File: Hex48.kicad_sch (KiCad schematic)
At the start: 0 parts

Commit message: Begin adding schematic.
Board is much better designed by using a proper schematic instead of just a PCB. But to do that, we need lots of generic connectors, all connected together in a way that only makes sense on the physical PCB layout. Oh well, make a start.
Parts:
- added D1, D2: LED, LED_THT:LED_D10.0mm, symbol Device:LED
- added H1, H2, H3, H4, H5, H6: MountingHole, MountingHole:MountingHole_3.2mm_M3_Pad_TopBottom, symbol Mechanical:MountingHole
- added J1: Conn_02x24_Counter_Clockwise, Package_DIP:DIP-48_W15.24mm_Socket_LongPads, symbol Connector_Generic:Conn_02x24_Counter_Clockwise
- added J2, J3, J6: Conn_02x24_Odd_Even, Connector_PinSocket_2.54mm:PinSocket_2x24_P2.54mm_Vertical, symbol Connector_Generic:Conn_02x24_Odd_Even
- added J4, J5: Conn_02x02_Odd_Even, Connector_PinSocket_2.54mm:PinSocket_2x02_P2.54mm_Vertical, symbol Connector_Generic:Conn_02x02_Odd_Even
- added SW1, SW2: SW_Push, Button_Switch_THT:SW_PUSH_6mm, symbol Switch:SW_Push
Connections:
- new net: D1.1 (K), J4.1 (Pin_1), J4.3 (Pin_3), SW1.1
- new net: D1.2 (A), J4.2 (Pin_2), J4.4 (Pin_4), SW1.2
- new net: D2.1 (K), J5.1 (Pin_1), J5.3 (Pin_3), SW2.1
- new net: D2.2 (A), J5.2 (Pin_2), J5.4 (Pin_4), SW2.2
- new net: J1.40 (Pin_40), J2.17 (Pin_17), J2.18 (Pin_18)
- new net: J1.39 (Pin_39), J2.19 (Pin_19), J2.20 (Pin_20)
- new net: J1.38 (Pin_38), J2.21 (Pin_21), J2.22 (Pin_22)
- new net: J1.37 (Pin_37), J2.23 (Pin_23), J2.24 (Pin_24)
- new net: J1.36 (Pin_36), J2.25 (Pin_25), J2.26 (Pin_26)
- new net: J1.35 (Pin_35), J2.27 (Pin_27), J2.28 (Pin_28)
- new net: J1.34 (Pin_34), J2.29 (Pin_29), J2.30 (Pin_30)
- new net: J1.33 (Pin_33), J2.31 (Pin_31), J2.32 (Pin_32)
- new net: J1.32 (Pin_32), J2.33 (Pin_33), J2.34 (Pin_34)
- new net: J1.31 (Pin_31), J2.35 (Pin_35), J2.36 (Pin_36)
- new net: J1.30 (Pin_30), J2.37 (Pin_37), J2.38 (Pin_38)
- new net: J1.29 (Pin_29), J2.39 (Pin_39), J2.40 (Pin_40)
- new net: J1.28 (Pin_28), J2.41 (Pin_41), J2.42 (Pin_42)
- new net: J1.27 (Pin_27), J2.43 (Pin_43), J2.44 (Pin_44)
- new net: J1.26 (Pin_26), J2.45 (Pin_45), J2.46 (Pin_46)
- new net: J1.25 (Pin_25), J2.47 (Pin_47), J2.48 (Pin_48)
- new net: J1.9 (Pin_9), J3.17 (Pin_17), J3.18 (Pin_18)
- new net: J1.10 (Pin_10), J3.19 (Pin_19), J3.20 (Pin_20)
- new net: J1.11 (Pin_11), J3.21 (Pin_21), J3.22 (Pin_22)
- new net: J1.12 (Pin_12), J3.23 (Pin_23), J3.24 (Pin_24)
- new net: J1.13 (Pin_13), J3.25 (Pin_25), J3.26 (Pin_26)
- new net: J1.14 (Pin_14), J3.27 (Pin_27), J3.28 (Pin_28)
- new net: J1.15 (Pin_15), J3.29 (Pin_29), J3.30 (Pin_30)
- new net: J1.16 (Pin_16), J3.31 (Pin_31), J3.32 (Pin_32)
- new net: J1.17 (Pin_17), J3.33 (Pin_33), J3.34 (Pin_34)
- new net: J1.18 (Pin_18), J3.35 (Pin_35), J3.36 (Pin_36)
- new net: J1.19 (Pin_19), J3.37 (Pin_37), J3.38 (Pin_38)
- new net: J1.20 (Pin_20), J3.39 (Pin_39), J3.40 (Pin_40)
- new net: J1.21 (Pin_21), J3.41 (Pin_41), J3.42 (Pin_42)
- new net: J1.22 (Pin_22), J3.43 (Pin_43), J3.44 (Pin_44)
- new net: J1.23 (Pin_23), J3.45 (Pin_45), J3.46 (Pin_46)
- new net: J1.24 (Pin_24), J3.47 (Pin_47), J3.48 (Pin_48)
- new net pin1: J1.1 (Pin_1), J3.1 (Pin_1), J3.2 (Pin_2), J6.2 (Pin_2)
- new net pin2: J1.2 (Pin_2), J3.3 (Pin_3), J3.4 (Pin_4), J6.4 (Pin_4)
- new net pin3: J1.3 (Pin_3), J3.5 (Pin_5), J3.6 (Pin_6), J6.6 (Pin_6)
- new net pin4: J1.4 (Pin_4), J3.7 (Pin_7), J3.8 (Pin_8), J6.8 (Pin_8)
- new net pin41: J1.41 (Pin_41), J2.15 (Pin_15), J2.16 (Pin_16), J6.15 (Pin_15)
- new net pin42: J1.42 (Pin_42), J2.13 (Pin_13), J2.14 (Pin_14), J6.13 (Pin_13)
- new net pin43: J1.43 (Pin_43), J2.11 (Pin_11), J2.12 (Pin_12), J6.11 (Pin_11)
- new net pin44: J1.44 (Pin_44), J2.10 (Pin_10), J2.9 (Pin_9), J6.9 (Pin_9)
- new net pin45: J1.45 (Pin_45), J2.7 (Pin_7), J2.8 (Pin_8), J6.7 (Pin_7)
- new net pin46: J1.46 (Pin_46), J2.5 (Pin_5), J2.6 (Pin_6), J6.5 (Pin_5)
- new net pin47: J1.47 (Pin_47), J2.3 (Pin_3), J2.4 (Pin_4), J6.3 (Pin_3)
- new net pin48: J1.48 (Pin_48), J2.1 (Pin_1), J2.2 (Pin_2), J6.1 (Pin_1)
- new net pin5: J1.5 (Pin_5), J3.10 (Pin_10), J3.9 (Pin_9), J6.10 (Pin_10)
- new net pin6: J1.6 (Pin_6), J3.11 (Pin_11), J3.12 (Pin_12), J6.12 (Pin_12)
- new net pin7: J1.7 (Pin_7), J3.13 (Pin_13), J3.14 (Pin_14), J6.14 (Pin_14)
- new net pin8: J1.8 (Pin_8), J3.15 (Pin_15), J3.16 (Pin_16), J6.16 (Pin_16)

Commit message: Add title block info.
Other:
- company: (none) -> John Honniball
- title: (none) -> Hex48 Prototyping Board
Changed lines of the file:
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@@
 	(generator_version "8.0")
 	(paper "A4")
+	(title_block
+		(title "Hex48 Prototyping Board")
+		(date "2024-10-09")
+		(rev "0.2")
+		(company "John Honniball")
+		(comment 1 "Hexagonal DIL breadboard")
+	)
 	(junction
 		(at 106.68 76.2)

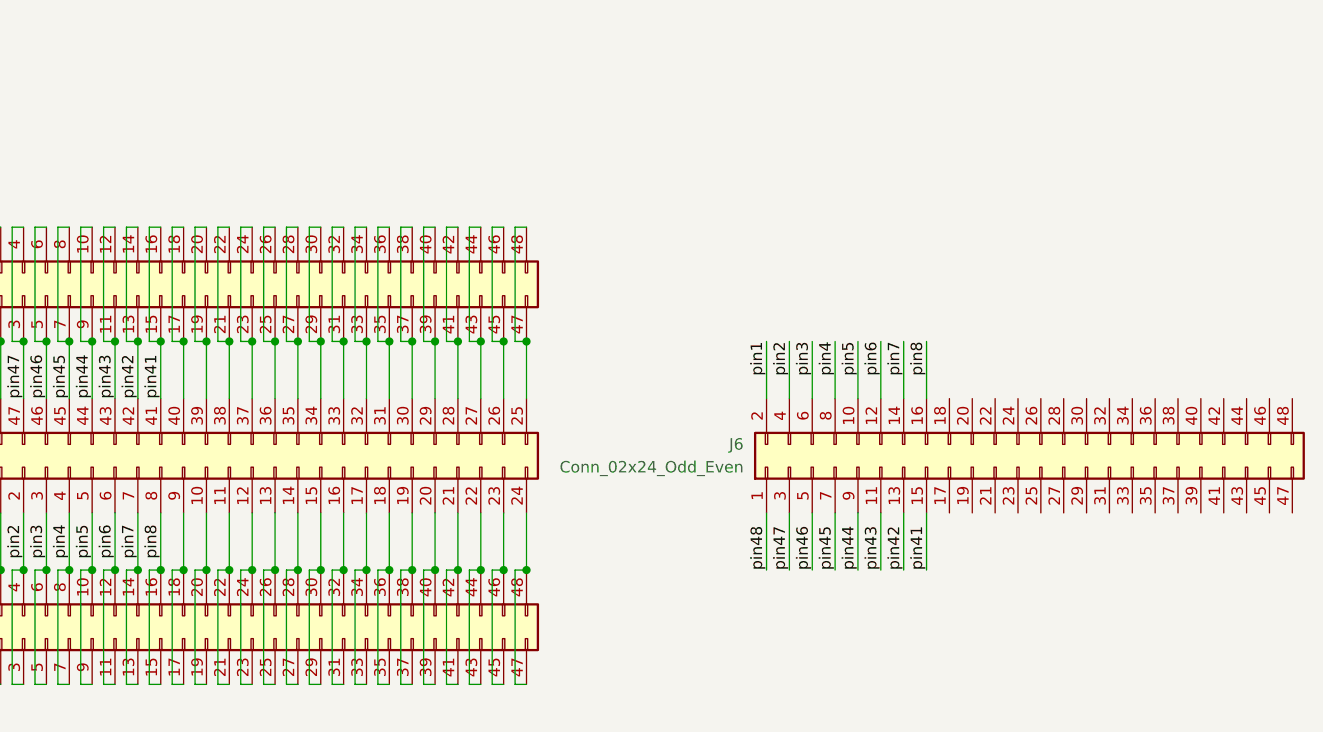
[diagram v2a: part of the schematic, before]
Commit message: Finish DIL wiring.
Place two 24-pin narrow DIL sockets and connect them to the 48-pin wide DIL socket. Name all pin signals.
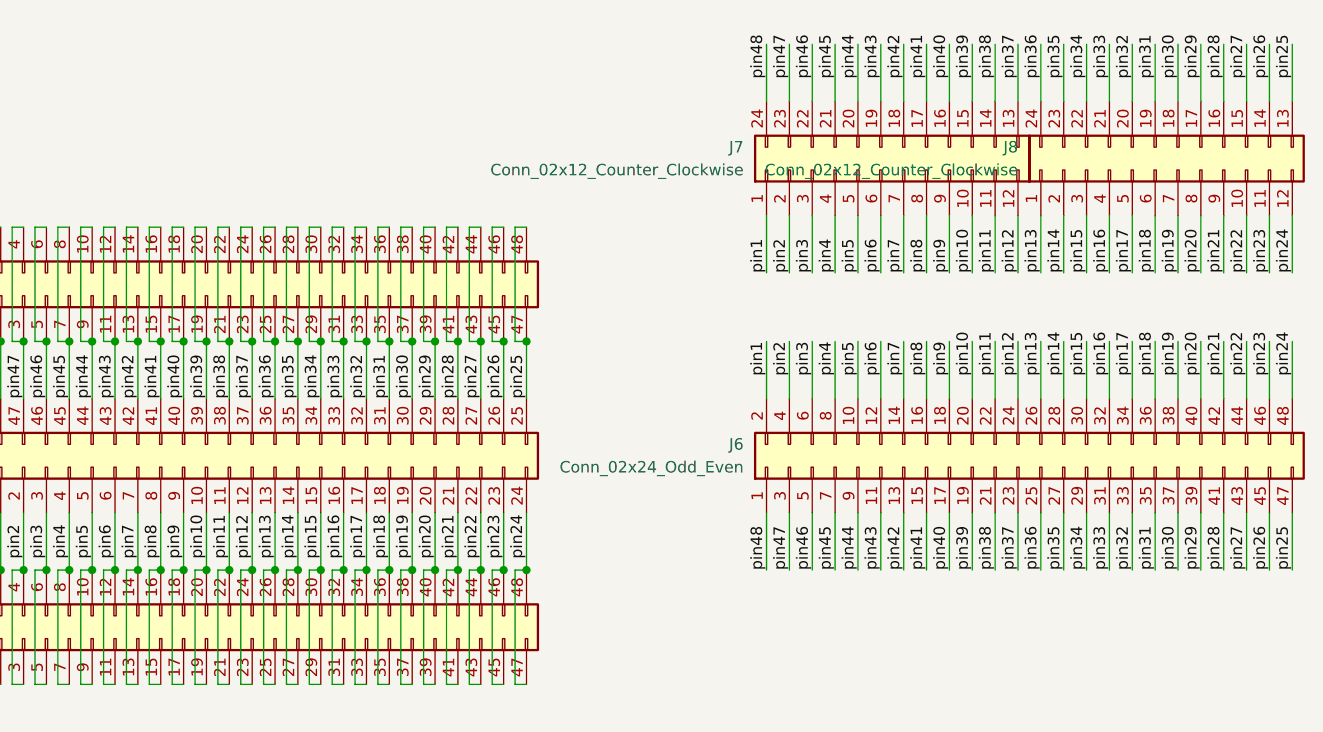
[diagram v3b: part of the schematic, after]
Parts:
- added J7, J8: Conn_02x12_Counter_Clockwise, Package_DIP:DIP-24_W7.62mm_Socket_LongPads, symbol Connector_Generic:Conn_02x12_Counter_Clockwise
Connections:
- net pin1: now also J7.1 (Pin_1)
- net pin2: now also J7.2 (Pin_2)
- net pin3: now also J7.3 (Pin_3)
- net pin4: now also J7.4 (Pin_4)
- net pin41: now also J7.17 (Pin_17)
- net pin42: now also J7.18 (Pin_18)
- net pin43: now also J7.19 (Pin_19)
- net pin44: now also J7.20 (Pin_20)
- net pin45: now also J7.21 (Pin_21)
- net pin46: now also J7.22 (Pin_22)
- net pin47: now also J7.23 (Pin_23)
- net pin48: now also J7.24 (Pin_24)
- net pin5: now also J7.5 (Pin_5)
- net pin6: now also J7.6 (Pin_6)
- net pin7: now also J7.7 (Pin_7)
- net pin8: now also J7.8 (Pin_8)
- net pin40: now reaches J6.17 (Pin_17)
- net pin40: now also J1.40 (Pin_40), J2.17 (Pin_17), J2.18 (Pin_18), J7.16 (Pin_16)
- net pin9: now reaches J6.18 (Pin_18)
- net pin9: now also J1.9 (Pin_9), J3.17 (Pin_17), J3.18 (Pin_18), J7.9 (Pin_9)
- net pin39: now reaches J6.19 (Pin_19)
- net pin39: now also J1.39 (Pin_39), J2.19 (Pin_19), J2.20 (Pin_20), J7.15 (Pin_15)
- net pin10: now reaches J6.20 (Pin_20)
- net pin10: now also J1.10 (Pin_10), J3.19 (Pin_19), J3.20 (Pin_20), J7.10 (Pin_10)
- net pin38: now reaches J6.21 (Pin_21)
- net pin38: now also J1.38 (Pin_38), J2.21 (Pin_21), J2.22 (Pin_22), J7.14 (Pin_14)
- net pin11: now reaches J6.22 (Pin_22)
- net pin11: now also J1.11 (Pin_11), J3.21 (Pin_21), J3.22 (Pin_22), J7.11 (Pin_11)
- net pin37: now reaches J6.23 (Pin_23)
- net pin37: now also J1.37 (Pin_37), J2.23 (Pin_23), J2.24 (Pin_24), J7.13 (Pin_13)
- net pin12: now reaches J6.24 (Pin_24)
- net pin12: now also J1.12 (Pin_12), J3.23 (Pin_23), J3.24 (Pin_24), J7.12 (Pin_12)
- net pin36: now reaches J6.25 (Pin_25)
- net pin36: now also J1.36 (Pin_36), J2.25 (Pin_25), J2.26 (Pin_26), J8.24 (Pin_24)
- net pin13: now reaches J6.26 (Pin_26)
- net pin13: now also J1.13 (Pin_13), J3.25 (Pin_25), J3.26 (Pin_26), J8.1 (Pin_1)
- net pin35: now reaches J6.27 (Pin_27)
- net pin35: now also J1.35 (Pin_35), J2.27 (Pin_27), J2.28 (Pin_28), J8.23 (Pin_23)
- net pin14: now reaches J6.28 (Pin_28)
- net pin14: now also J1.14 (Pin_14), J3.27 (Pin_27), J3.28 (Pin_28), J8.2 (Pin_2)
- net pin34: now reaches J6.29 (Pin_29)
- net pin34: now also J1.34 (Pin_34), J2.29 (Pin_29), J2.30 (Pin_30), J8.22 (Pin_22)
- net pin15: now reaches J6.30 (Pin_30)
- net pin15: now also J1.15 (Pin_15), J3.29 (Pin_29), J3.30 (Pin_30), J8.3 (Pin_3)
- net pin33: now reaches J6.31 (Pin_31)
- net pin33: now also J1.33 (Pin_33), J2.31 (Pin_31), J2.32 (Pin_32), J8.21 (Pin_21)
- net pin16: now reaches J6.32 (Pin_32)
- net pin16: now also J1.16 (Pin_16), J3.31 (Pin_31), J3.32 (Pin_32), J8.4 (Pin_4)
- net pin32: now reaches J6.33 (Pin_33)
- net pin32: now also J1.32 (Pin_32), J2.33 (Pin_33), J2.34 (Pin_34), J8.20 (Pin_20)
- net pin17: now reaches J6.34 (Pin_34)
- net pin17: now also J1.17 (Pin_17), J3.33 (Pin_33), J3.34 (Pin_34), J8.5 (Pin_5)
- net pin31: now reaches J6.35 (Pin_35)
- net pin31: now also J1.31 (Pin_31), J2.35 (Pin_35), J2.36 (Pin_36), J8.19 (Pin_19)
- net pin18: now reaches J6.36 (Pin_36)
- net pin18: now also J1.18 (Pin_18), J3.35 (Pin_35), J3.36 (Pin_36), J8.6 (Pin_6)
- net pin30: now reaches J6.37 (Pin_37)
- net pin30: now also J1.30 (Pin_30), J2.37 (Pin_37), J2.38 (Pin_38), J8.18 (Pin_18)
- net pin19: now reaches J6.38 (Pin_38)
- net pin19: now also J1.19 (Pin_19), J3.37 (Pin_37), J3.38 (Pin_38), J8.7 (Pin_7)
- net pin29: now reaches J6.39 (Pin_39)
- net pin29: now also J1.29 (Pin_29), J2.39 (Pin_39), J2.40 (Pin_40), J8.17 (Pin_17)
- net pin20: now reaches J6.40 (Pin_40)
- net pin20: now also J1.20 (Pin_20), J3.39 (Pin_39), J3.40 (Pin_40), J8.8 (Pin_8)
- net pin28: now reaches J6.41 (Pin_41)
- net pin28: now also J1.28 (Pin_28), J2.41 (Pin_41), J2.42 (Pin_42), J8.16 (Pin_16)
- net pin21: now reaches J6.42 (Pin_42)
- net pin21: now also J1.21 (Pin_21), J3.41 (Pin_41), J3.42 (Pin_42), J8.9 (Pin_9)
- net pin27: now reaches J6.43 (Pin_43)
- net pin27: now also J1.27 (Pin_27), J2.43 (Pin_43), J2.44 (Pin_44), J8.15 (Pin_15)
- net pin22: now reaches J6.44 (Pin_44)
- net pin22: now also J1.22 (Pin_22), J3.43 (Pin_43), J3.44 (Pin_44), J8.10 (Pin_10)
- net pin26: now reaches J6.45 (Pin_45)
- net pin26: now also J1.26 (Pin_26), J2.45 (Pin_45), J2.46 (Pin_46), J8.14 (Pin_14)
- net pin23: now reaches J6.46 (Pin_46)
- net pin23: now also J1.23 (Pin_23), J3.45 (Pin_45), J3.46 (Pin_46), J8.11 (Pin_11)
- net pin25: now reaches J6.47 (Pin_47)
- net pin25: now also J1.25 (Pin_25), J2.47 (Pin_47), J2.48 (Pin_48), J8.13 (Pin_13)
- net pin24: now reaches J6.48 (Pin_48)
- net pin24: now also J1.24 (Pin_24), J3.47 (Pin_47), J3.48 (Pin_48), J8.12 (Pin_12)
